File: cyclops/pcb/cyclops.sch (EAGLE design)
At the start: 155 parts, among them Q1 BC817, Q2 IRF510, Q3 BC817, Q4 BC817, U1 MCP4921, U10 TLV2374, U11 THS4281, U12 MAX4564, U13 ZXTD, U14 ZXTD, U3 MAX4564, U4 LT1931, U5 LT1764A, U6 337L, U67 ZLDO1117, U69 LT1716, U7 TLV3701, U8 ADR03, U9 OP1177

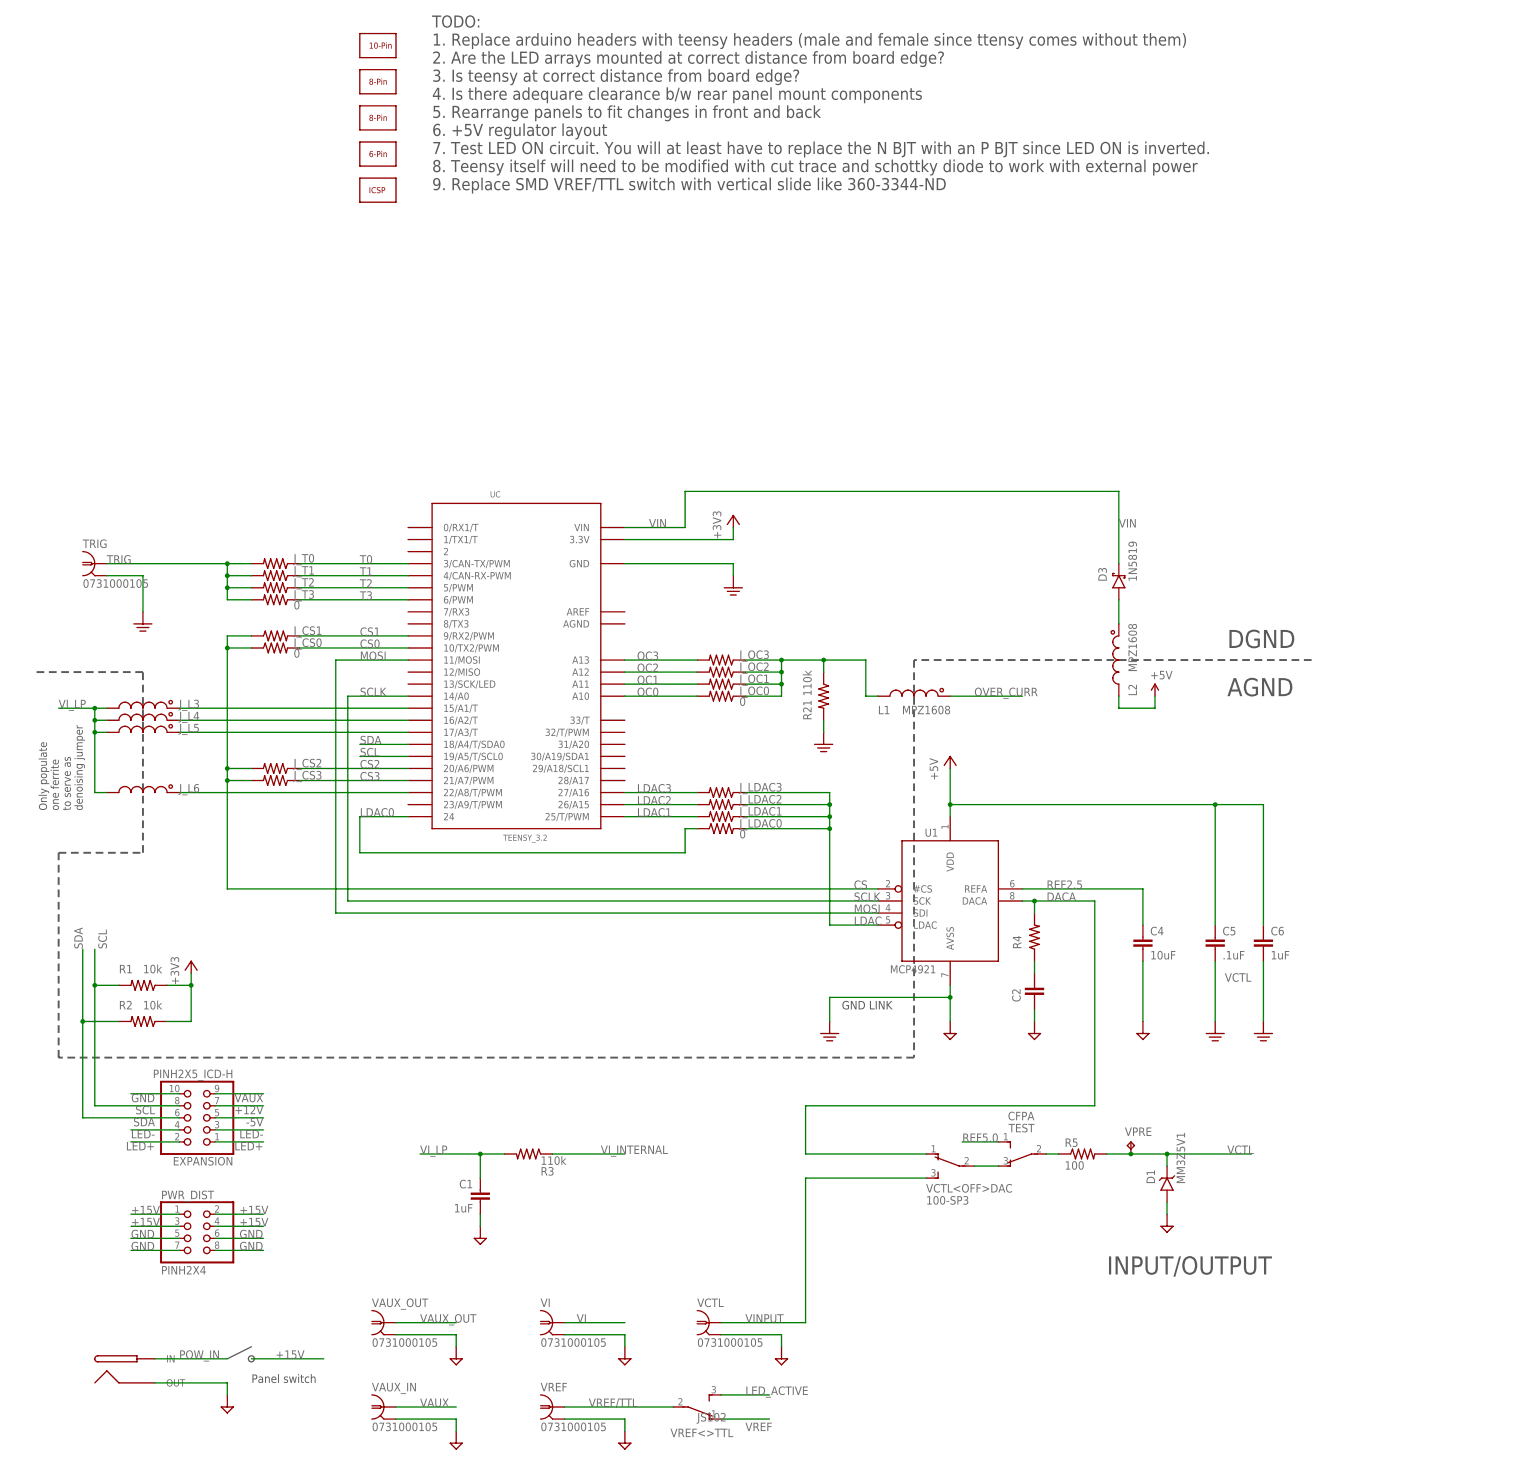
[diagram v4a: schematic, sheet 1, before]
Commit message: Ticking off preparations for 3.6 layout.
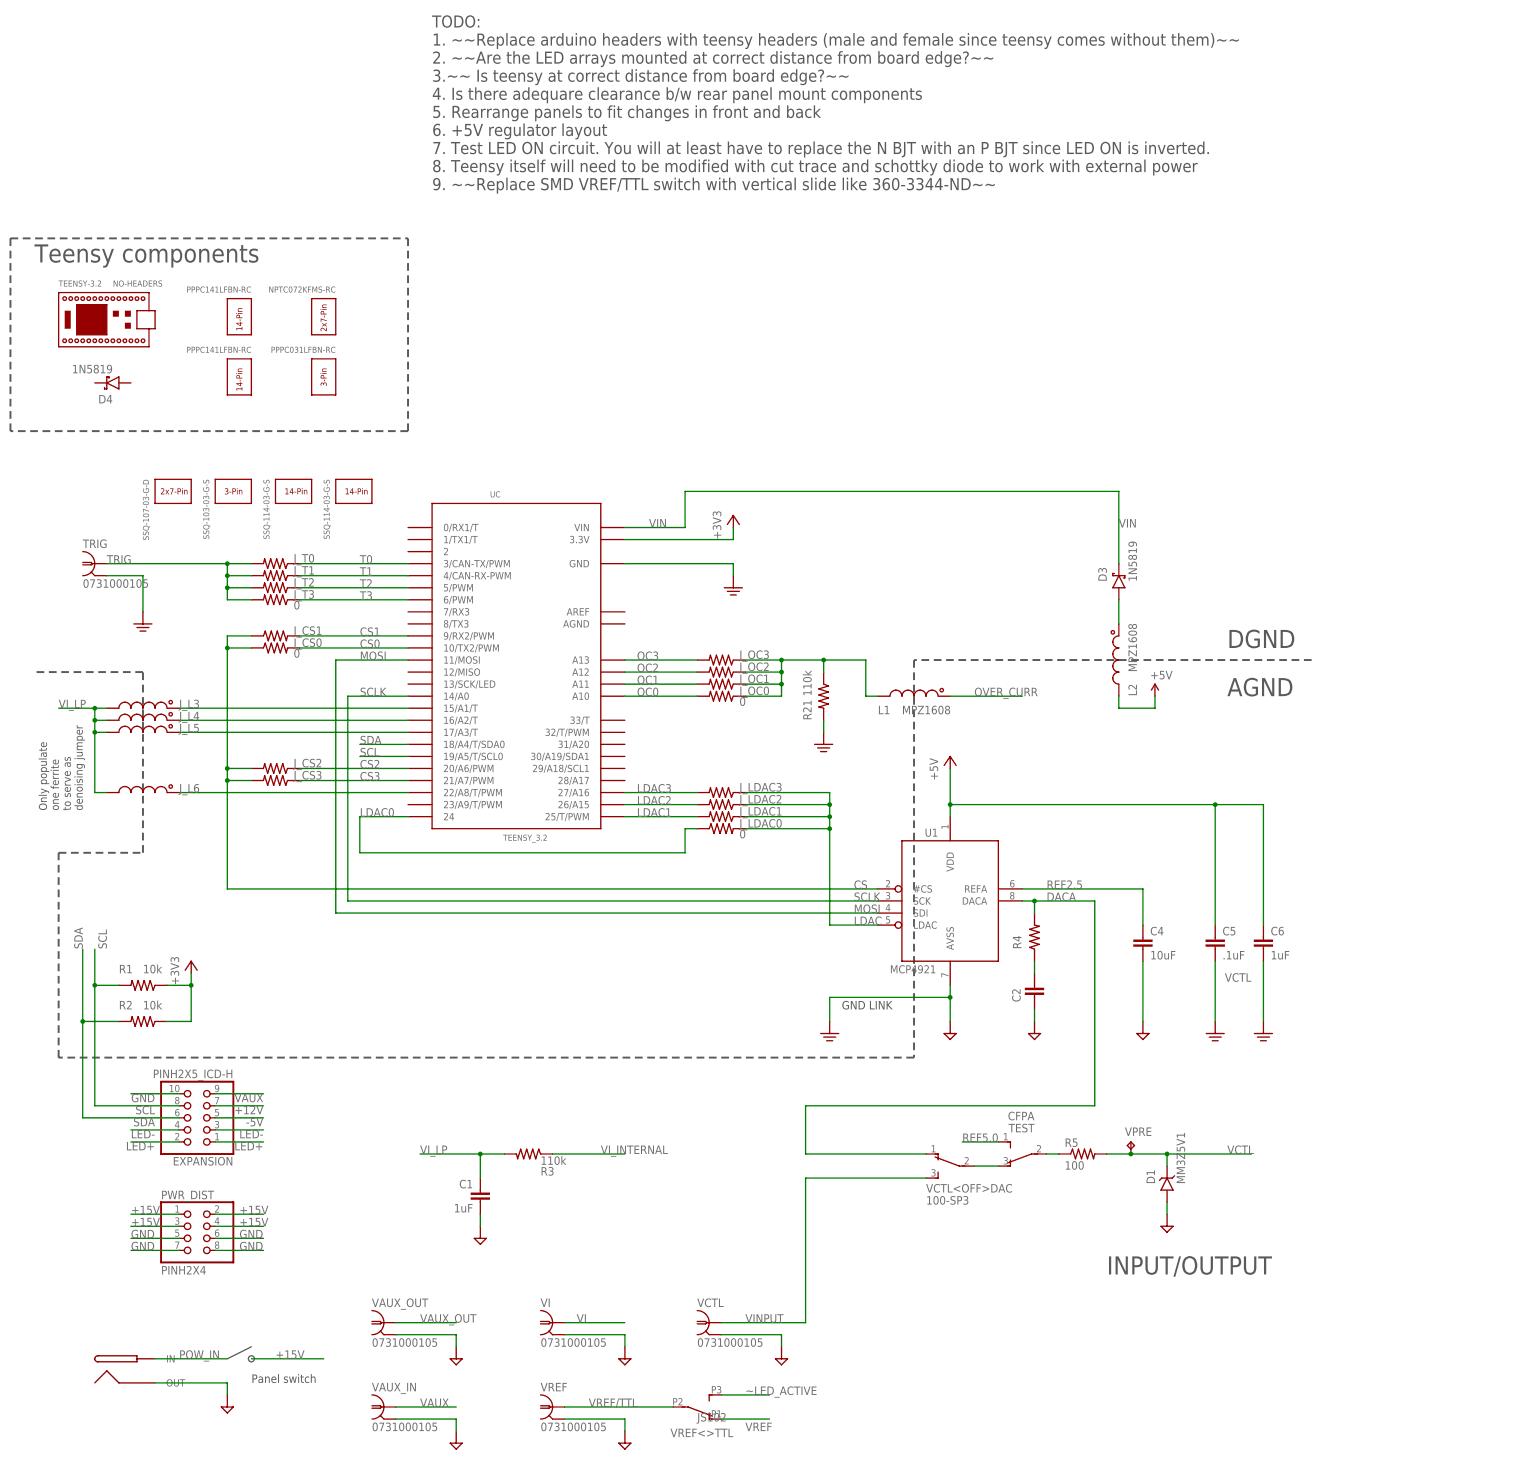
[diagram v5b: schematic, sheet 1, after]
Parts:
- added D4: 1N5819, jonnew:S-DIODESOD-123
- VREF<>TTL: device cyclops:SPDT_JS -> jonnew:SPDT_AS12A*
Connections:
- removed net LED_ACTIVE: VREF<>TTL.3
- net ~LED_ACTIVE: now also VREF<>TTL.3
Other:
- note added: "TODO: 1. ~~Replace arduino headers with teensy headers (male and female since teensy comes without them)~~ 2. ~~Are the LED arrays mounted at correct distance from board edge?~~ 3.~~ Is teensy at correct distance from board edge?~~ 4. Is there adequare clearance b/w rear panel mount components 5. Rearrange panels to fit changes in front and back 6. +5V regulator layout 7. Test LED ON circuit. You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"
- note added: "Teensy components"
- note removed: "TODO: 1. Replace arduino headers with teensy headers (male and female since ttensy comes without them) 2. Are the LED arrays mounted at correct distance from board edge? 3. Is teensy at correct distance from board edge? 4. Is there adequare clearance b/w rear panel mount components 5. Rearrange panels to fit changes in front and back 6. +5V regulator layout 7. Test LED ON circuit. You will at lea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"
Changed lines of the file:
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@@
 <setting verticaltext="up"/>
 </settings>
-<grid distance="0.1" unitdist="inch" unit="inch" style="lines" multiple="1" display="yes" altdistance="0.01" altunitdist="inch" altunit="inch"/>
+<grid distance="0.1" unitdist="inch" unit="inch" style="lines" multiple="1" display="no" altdistance="0.01" altunitdist="inch" altunit="inch"/>
 <layers>
 <layer number="1" name="Top" color="4" fill="1" visible="no" active="no"/>
@@
 <part name="TRIG" library="jonnew" deviceset="BNC" device="_0731000105" value="0731000105"/>
 <part name="U$47" library="cyclops" deviceset="GND1" device=""/>
-<part name="LEO-HEADERS" library="cyclops" deviceset="ARDUINO_HEADER_SET" device=""/>
 <part name="R16" library="cyclops" deviceset="R" device="_0603" value="1k"/>
 <part name="U$49" library="cyclops" deviceset="GND2" device=""/>
@@
 <part name="OC" library="jonnew" deviceset="LED_2X" device="_VERTICAL"/>
 <part name="D3" library="jonnew" deviceset="S-DIODE" device="SOD-123" value="1N5819"/>
-<part name="VREF&lt;&gt;TTL" library="cyclops" deviceset="SPDT" device="_JS" value="JS102"/>
+<part name="VREF&lt;&gt;TTL" library="jonnew" deviceset="SPDT" device="_AS12A*" value="JS102"/>
 <part name="C8" library="cyclops" deviceset="C" device="_0603" value=".1uF"/>
 <part name="R42" library="cyclops" deviceset="R" device="_0603" value="1k"/>
@@
 <part name="R45" library="cyclops" deviceset="R" device="_0603"/>
 <part name="U$28" library="cyclops" deviceset="GND2" device=""/>
+<part name="U$48" library="jonnew" deviceset="TEENSY-2X7-PIN-HEADER" device="" value="SSQ-107-03-G-D"/>
+<part name="U$54" library="jonnew" deviceset="TEENSY-3-PIN-HEADER" device="" value="SSQ-103-03-G-S"/>
+<part name="U$55" library="jonnew" deviceset="TEENSY-14-PIN-HEADER" device="" value="SSQ-114-03-G-S"/>
+<part name="U$63" library="jonnew" deviceset="TEENSY-14-PIN-HEADER" device="" value="SSQ-114-03-G-S"/>
+<part name="D4" library="jonnew" deviceset="S-DIODE" device="SOD-123" value="1N5819"/>
+<part name="U$66" library="jonnew" deviceset="TEENSY-2X7-PIN-HEADER" device="" value="NPTC072KFMS-RC"/>
+<part name="U$69" library="jonnew" deviceset="TEENSY-3-PIN-HEADER" device="" value="PPPC031LFBN-RC"/>
+<part name="U$72" library="jonnew" deviceset="TEENSY-14-PIN-HEADER" device="" value="PPPC141LFBN-RC"/>
+<part name="U$73" library="jonnew" deviceset="TEENSY-14-PIN-HEADER" device="" value="PPPC141LFBN-RC"/>
+<part name="TEENSY-3.2" library="jonnew" deviceset="TEENSY_SYMBOL" device="" value="NO-HEADERS"/>
 </parts>
 <sheets>
@@
 <wire x1="15.24" y1="99.06" x2="-7.62" y2="99.06" width="0.4064" layer="97" style="shortdash"/>
 <text x="76.2" y="200.66" size="2.54" layer="97">TODO:
-1. Replace arduino headers with teensy headers (male and female since ttensy comes without them)
-2. Are the LED arrays mounted at correct distance from board edge?
-3. Is teensy at correct distance from board edge?
+1. ~~Replace arduino headers with teensy headers (male and female since teensy comes without them)~~
+2. ~~Are the LED arrays mounted at correct distance from board edge?~~
+3.~~ Is teensy at correct distance from board edge?~~
 4. Is there adequare clearance b/w rear panel mount components
 5. Rearrange panels to fit changes in front and back
@@
 7. Test LED ON circuit. You will at least have to replace the N BJT with an P BJT since LED ON is inverted.
 8. Teensy itself will need to be modified with cut trace and schottky diode to work with external power
-9. Replace SMD VREF/TTL switch with vertical slide like 360‑3344‑ND</text>
+9. ~~Replace SMD VREF/TTL switch with vertical slide like 360‑3344‑ND~~</text>
+<wire x1="-12.7" y1="190.5" x2="71.12" y2="190.5" width="0.4064" layer="97" style="shortdash"/>
+<wire x1="71.12" y1="190.5" x2="71.12" y2="149.86" width="0.4064" layer="97" style="shortdash"/>
+<wire x1="71.12" y1="149.86" x2="-12.7" y2="149.86" width="0.4064" layer="97" style="shortdash"/>
+<wire x1="-12.7" y1="149.86" x2="-12.7" y2="190.5" width="0.4064" layer="97" style="shortdash"/>
+<text x="-7.62" y="185.42" size="3.81" layer="97">Teensy components</text>
 </plain>
 <instances>
@@
 <instance part="TRIG" gate="G$1" x="5.08" y="121.92"/>
 <instance part="U$47" gate="G$1" x="15.24" y="109.22"/>
-<instance part="LEO-HEADERS" gate="G$1" x="60.96" y="205.74"/>
-<instance part="LEO-HEADERS" gate="G$2" x="60.96" y="228.6"/>
-<instance part="LEO-HEADERS" gate="G$3" x="60.96" y="220.98"/>
-<instance part="LEO-HEADERS" gate="G$4" x="60.96" y="213.36"/>
 <instance part="J_L3" gate="L" x="15.24" y="91.44" smashed="yes" rot="R270">
 <attribute name="NAME" x="22.86" y="91.44" size="1.778" layer="95"/>
@@
 <instance part="POWER" gate="G$1" x="20.32" y="-48.26" rot="MR0"/>
 <instance part="U$11" gate="G$1" x="33.02" y="-55.88"/>
-<instance part="LEO-HEADERS" gate="G$5" x="60.96" y="198.12"/>
 <instance part="SUPPLY10" gate="G$1" x="228.6" y="93.98"/>
 <instance part="R5" gate="R" x="213.36" y="-2.54"/>
@@
 <attribute name="VALUE" x="175.26" y="90.17" size="1.778" layer="96"/>
 </instance>
+<instance part="U$48" gate="G$1" x="17.78" y="134.62"/>
+<instance part="U$54" gate="G$1" x="30.48" y="134.62"/>
+<instance part="U$55" gate="G$1" x="43.18" y="134.62"/>
+<instance part="U$63" gate="G$1" x="55.88" y="134.62"/>
+<instance part="D4" gate="G$1" x="7.62" y="160.02" rot="R180"/>
+<instance part="U$66" gate="G$1" x="50.8" y="177.8" rot="R270"/>
+<instance part="U$69" gate="G$1" x="50.8" y="165.1" rot="R270"/>
+<instance part="U$72" gate="G$1" x="33.02" y="177.8" rot="R270"/>
+<instance part="U$73" gate="G$1" x="33.02" y="165.1" rot="R270"/>
+<instance part="TEENSY-3.2" gate="G$1" x="-2.54" y="167.64"/>
 </instances>
 <busses>
@@
 </segment>
 </net>
-<net name="LED_ACTIVE" class="0">
+<net name="~LED_ACTIVE" class="0">
 <segment>
 <pinref part="VREF&lt;&gt;TTL" gate="G$1" pin="3"/>
